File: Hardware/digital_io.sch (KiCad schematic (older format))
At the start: 8 parts, among them Q34 NX7002AK, SW23 SW_Push, SW24 SW_Push, SW25 EC12E24204A9, SW26 EC12E24204A9

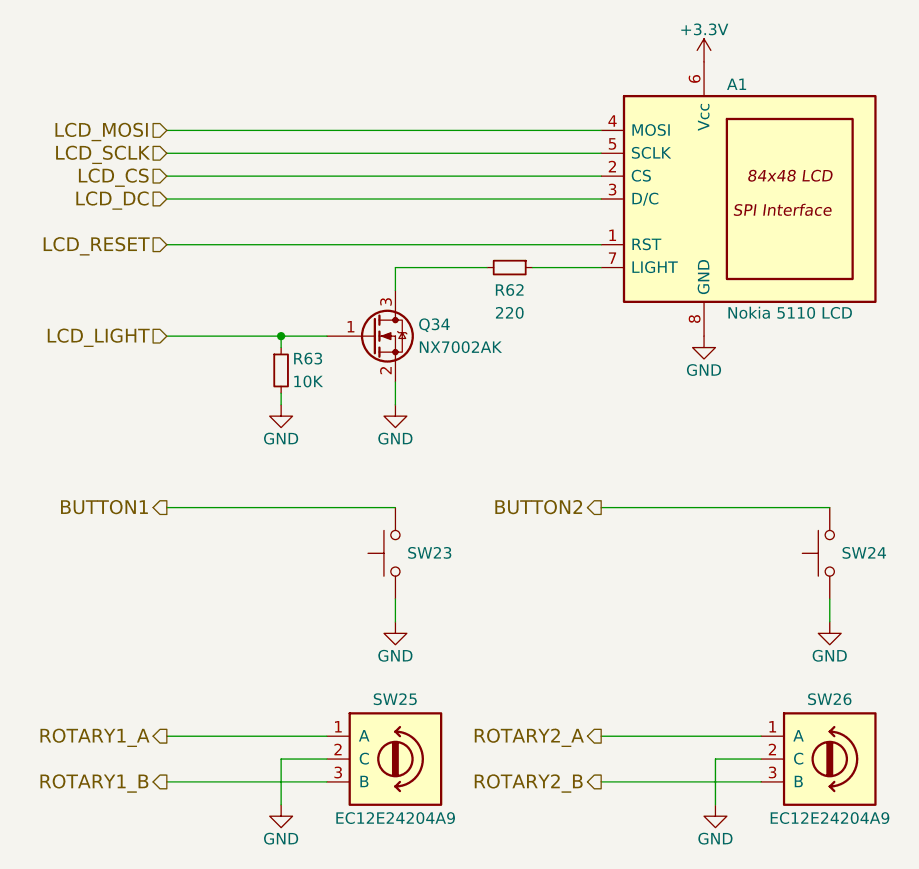
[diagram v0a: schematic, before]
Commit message: linked footprints with 3D models in project directory
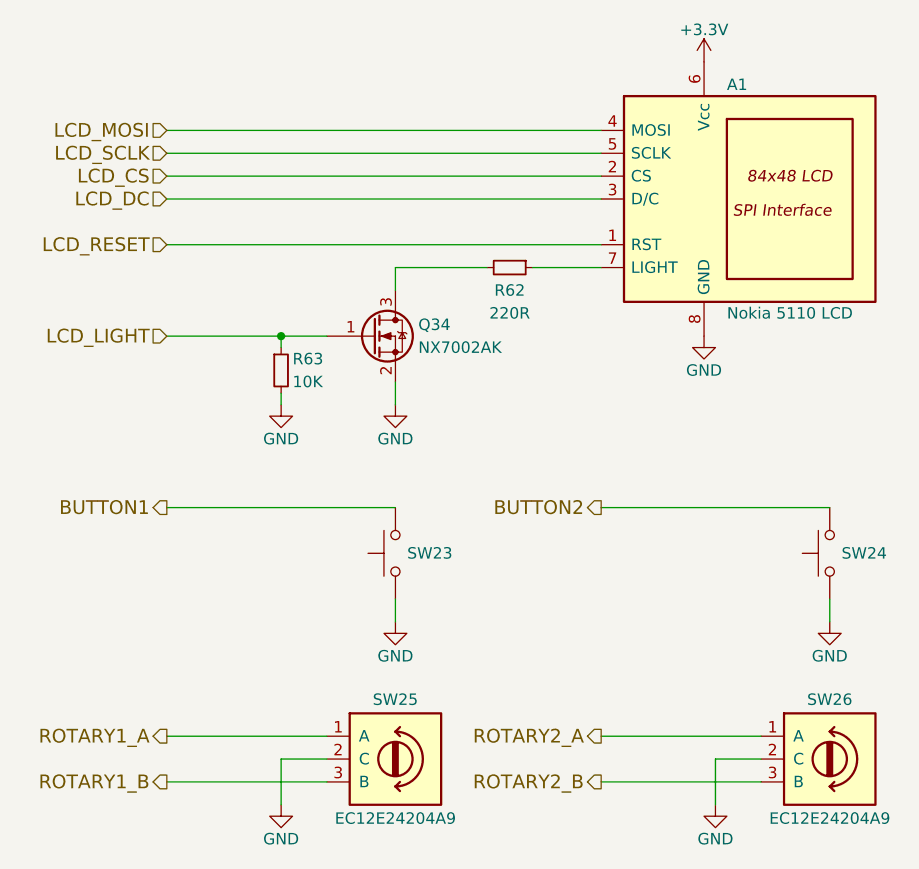
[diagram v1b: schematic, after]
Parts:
- A1: Catalog link (none) -> https://www.ebay.com/itm/84-48-LCD-Module-White-Backlight-A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
- R62: value 220 -> 220R
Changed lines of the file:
@@
 F 2 "project_library:Nokia_5110_lcd" H 6650 3200 50  0001 C CNN
 F 3 "" H 6750 3300 50  0001 C CNN
+F 4 "https://www.ebay.com/itm/84-48-LCD-Module-White-Backlight-Adapter-PCB-for-Nokia-5110-Arduino/400488314619" H 7400 2800 60  0001 C CNN "Catalog link"
 	1    7400 2800
 	1    0    0    -1
@@
 P 6200 3100
 F 0 "R62" V 6300 3100 50  0000 C CNN
-F 1 "220" V 6400 3100 50  0000 C CNN
+F 1 "220R" V 6400 3100 50  0000 C CNN
 F 2 "project_library:R_0603" H 6200 3100 50  0001 C CNN
 F 3 "" H 6200 3100 50  0001 C CNN

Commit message: converted all components except big tactile switches
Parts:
- A1: symbol lcd_nokia_5110 -> project_library:lcd_nokia_5110
- Q34: symbol 2N7002 -> project_library:2N7002
- R62, R63: symbol R_Small -> project_library:R_Small
- SW23, SW24: symbol SW_Push -> project_library:SW_Push
- SW25, SW26: symbol Rotary_Encoder -> project_library:Rotary_Encoder
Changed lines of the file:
@@
-EESchema Schematic File Version 2
-LIBS:project_library
-LIBS:power
-LIBS:device
-LIBS:switches
-LIBS:relays
-LIBS:motors
-LIBS:transistors
-LIBS:conn
-LIBS:linear
-LIBS:regul
-LIBS:74xx
-LIBS:cmos4000
-LIBS:adc-dac
-LIBS:memory
-LIBS:xilinx
-LIBS:microcontrollers
-LIBS:diode
-LIBS:dsp
-LIBS:microchip
-LIBS:analog_switches
-LIBS:motorola
-LIBS:texas
-LIBS:intel
-LIBS:audio
-LIBS:interface
-LIBS:digital-audio
-LIBS:philips
-LIBS:display
-LIBS:cypress
-LIBS:siliconi
-LIBS:opto
-LIBS:atmel
-LIBS:contrib
-LIBS:valves
-LIBS:stm32
-LIBS:ESD_Protection
+EESchema Schematic File Version 4
 LIBS:midi_grid-cache
-EELAYER 25 0
+EELAYER 30 0
 EELAYER END
 $Descr A4 11693 8268
@@
 $EndDescr
 $Comp
-L Rotary_Encoder SW25
+L project_library:Rotary_Encoder SW25
 U 1 1 5A3979F5
 P 5700 5250
@@
 $EndComp
 $Comp
-L GND #PWR0129
+L project_library:GND #PWR0129
 U 1 1 5A397ADE
 P 5200 5450
@@
 $EndComp
 $Comp
-L SW_Push SW23
+L project_library:SW_Push SW23
 U 1 1 5A39D16C
 P 5700 4350
@@
 ROTARY1_B
 $Comp
-L GND #PWR0130
+L project_library:GND #PWR0130
 U 1 1 5A39D52F
 P 5700 4650
@@
 BUTTON1
 $Comp
-L Rotary_Encoder SW26
+L project_library:Rotary_Encoder SW26
 U 1 1 5A39DA31
 P 7600 5250
@@
 $EndComp
 $Comp
-L GND #PWR0131
+L project_library:GND #PWR0131
 U 1 1 5A39DA37
 P 7100 5450
@@
 $EndComp
 $Comp
-L SW_Push SW24
+L project_library:SW_Push SW24
 U 1 1 5A39DA5F
 P 7600 4350
@@
 ROTARY2_B
 $Comp
-L GND #PWR0132
+L project_library:GND #PWR0132
 U 1 1 5A39DA67
 P 7600 4650
@@
 BUTTON2
 $Comp
-L lcd_nokia_5110 A1
+L project_library:lcd_nokia_5110 A1
 U 1 1 5A1F0214
 P 7400 2800
@@
 $EndComp
 $Comp
-L +3.3V #PWR0133
+L project_library:+3.3V #PWR0133
 U 1 1 5A1F0C1A
 P 7050 2200
@@
 $EndComp
 $Comp
-L GND #PWR0134
+L project_library:GND #PWR0134
 U 1 1 5A1F0FE5
 P 7050 3400
@@
 $EndComp
 $Comp
-L 2N7002 Q34
+L project_library:2N7002 Q34
 U 1 1 5A1F45C8
 P 5600 3400
@@
 $EndComp
 $Comp
-L R_Small R63
+L project_library:R_Small R63
 U 1 1 5A1F45CF
 P 5200 3550
@@
 $EndComp
 $Comp
-L GND #PWR0135
+L project_library:GND #PWR0135
 U 1 1 5A1F45D6
 P 5700 3700
@@
 $EndComp
 $Comp
-L GND #PWR0136
+L project_library:GND #PWR0136
 U 1 1 5A1F45DC
 P 5200 3700
@@
 	5700 3100 5700 3200
 $Comp
-L R_Small R62
+L project_library:R_Small R62
 U 1 1 5A52FA84
 P 6200 3100

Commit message: replaced all models with .step, deleted .wrl models
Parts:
- SW23: footprint project_library:Tactile_switch_12x12_black_cap -> project_library:Tactile_switch_12x12
- SW24: footprint project_library:Tactile_switch_12x12_red_cap -> project_library:Tactile_switch_12x12
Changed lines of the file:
@@
 F 0 "SW23" V 5700 4100 50  0000 L CNN
 F 1 "SW_Push" H 5700 4290 50  0001 C CNN
-F 2 "project_library:Tactile_switch_12x12_black_cap" H 5700 4550 50  0001 C CNN
+F 2 "project_library:Tactile_switch_12x12" H 5700 4550 50  0001 C CNN
 F 3 "" H 5700 4550 50  0001 C CNN
 	1    5700 4350
@@
 F 0 "SW24" V 7600 4100 50  0000 L CNN
 F 1 "SW_Push" H 7600 4290 50  0001 C CNN
-F 2 "project_library:Tactile_switch_12x12_red_cap" H 7600 4550 50  0001 C CNN
+F 2 "project_library:Tactile_switch_12x12" H 7600 4550 50  0001 C CNN
 F 3 "" H 7600 4550 50  0001 C CNN
 	1    7600 4350
@@
 	5700 4550 5700 4650
 Wire Wire Line
-	4700 3400 5400 3400
+	4700 3400 5200 3400
 Wire Wire Line
 	5200 3400 5200 3450
@@
 Wire Wire Line
 	6100 3100 5700 3100
+Wire Wire Line
+	5200 3400 5400 3400
 $EndSCHEMATC
